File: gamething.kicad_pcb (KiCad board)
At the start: 2 copper layers, 154 x 77.5 mm, 82 parts, among them J1 I2C Camera Connector, J2 MI0283QT-11, J3 Raspberry Pi Zero W, J4 SJ1-3524N, J5 USB_C_Receptacle_Power_Only, SW1 R, SW10 A, SW11 B, SW12 X, SW13 Y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

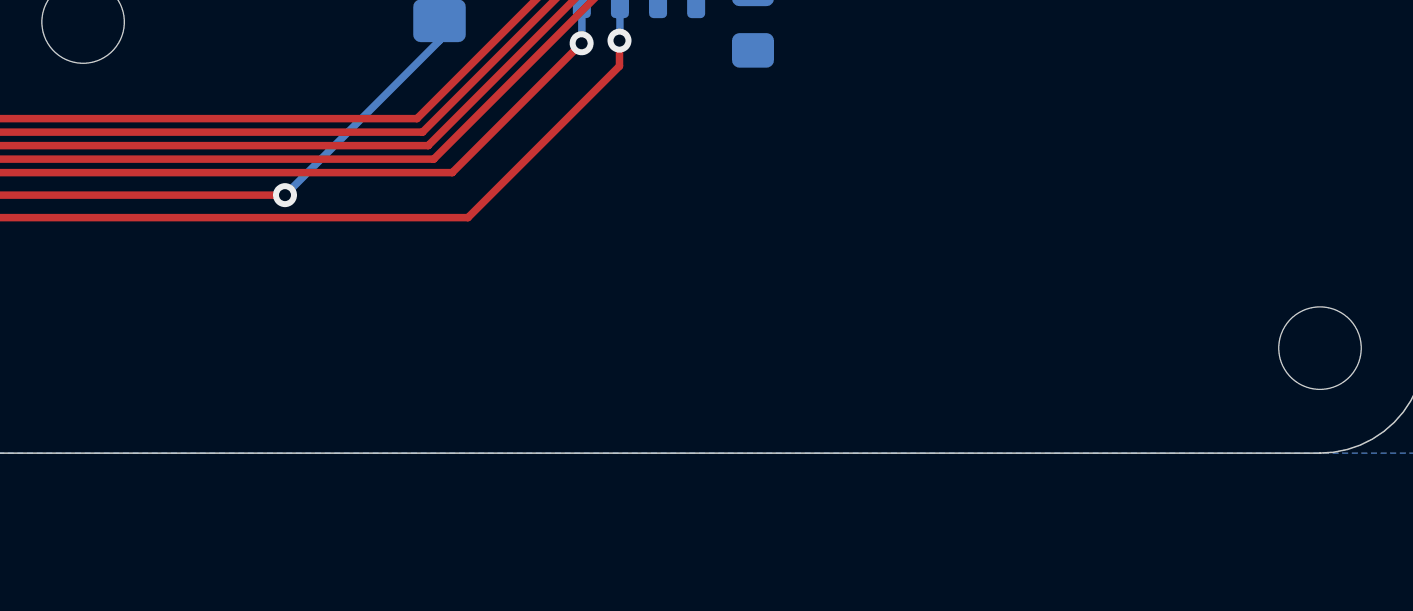
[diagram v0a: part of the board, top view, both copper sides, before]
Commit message: Add logo to board
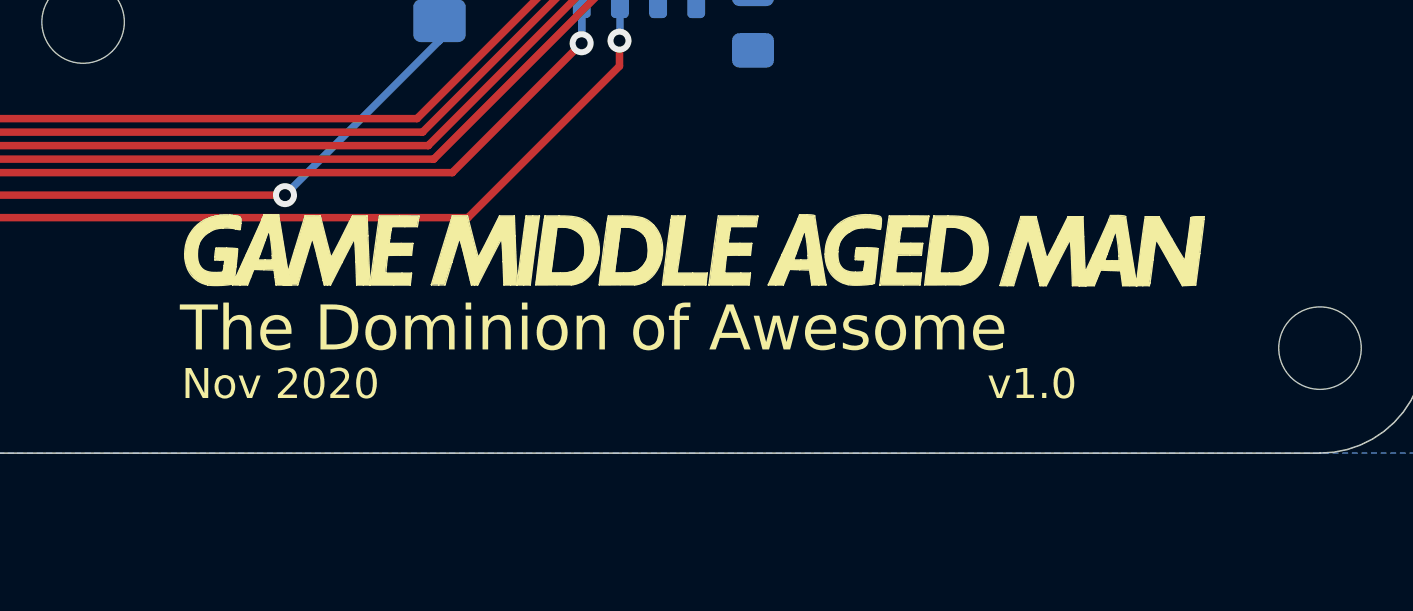
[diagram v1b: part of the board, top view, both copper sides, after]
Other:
- board text added: "Nov 2020"
- board text added: "The Dominion of Awesome"
- board text added: "v1.0"
